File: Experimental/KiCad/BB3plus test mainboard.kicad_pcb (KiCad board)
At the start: 4 copper layers, 180.5 x 176 mm, 292 parts, among them IC1 SN74HCS02PWR, IC10 TPS62933ODRLR, IC11 FUSB303BTMX, IC12 TPS2068E, IC13 RT9742SNGV, IC14 TPD4E001DRLR, IC15 TPD4E001DRLR, IC16 TPD12S016PWR, IC17 MIC2026A-1YM-TR, IC18 TPD4E001DRLR, IC2 TPS3851H18EDRBR, IC3 M24C32-DFDW6TP, IC4 STM32G071R8T6, IC5 TPA6205A1DGN, IC6 SN74LVC1G14DBVR, IC7 LM64460CPPQRYFRQ1, IC8 TPS62933ODRLR, IC9 USB5816C-I/KD, Q1 DMP3013SFV-7, Q2 2N7002, Q3 2N7002, Q4 MMBT5401, Q5 MMBT5401, Q6 2N7002, Q7 DMP3013SFV-7, Q8 DMP3013SFV-7, SW1 WBL2UOAGQR05CLR, SW2 LP4EE1RBATY, SW3 PEC16-2215F-S0024, X1 1-2199230-6, X10 1001878410201TLF, X11 77313-802-20LF, X12 77313-802-20LF, X13 10018783-10101TLF, X14 5051102091, X15 TBP03R1-350-10BE, X3 571-0400, X4 GSP1.9101.1, X5 PJ-002BH-SMT-TR, X6 USB4056-03-A, X7 0862-1J1T-43-F, X8 SS-53000-002, X9 5051102091, Y1 32.768KHz, Y2 VXM7-9032-25M0000000

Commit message: Jumpers update
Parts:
- added JP15: ~, PCM_EEZ_SMD:JP3 shorted with 0R (0603) 2-3, F.Cu at (397.3, 119.3)
- added JP16: ~, PCM_EEZ_SMD:JP3 shorted with 0R (0603) 2-3, F.Cu at (397.3, 120.6)
- JP14, JP2, JP6: value ~ -> 0R
- moved C7 3.13 mm to (397.5, 114.3), turned to 0 degrees
- moved IC3 2.31 mm to (395.2, 116.8)
- renumbered C39 to C38, C38 to C39, C49 to C47, C50 to C48, C47 to C49, C48 to C50, R40 to R39, R39 to R40
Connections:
- net I2C_PU_BIAS renamed CM5_3V3
- Module1 pad 143: unconnected-(Module1B-HDMI1_HOTPLUG-Pad143) -> TFT_DVID_HPA
- Module1 pad 145: unconnected-(Module1B-HDMI1_SDA-Pad145) -> TFT_DVID_SDA
- Module1 pad 147: unconnected-(Module1B-HDMI1_SCL-Pad147) -> TFT_DVID_SCL
- Module1 pad 149: unconnected-(Module1B-HDMI1_CEC-Pad149) -> TFT_DVID_CEC
- X9 pad 14: unconnected-(X9-CTRL1-Pad14) -> TFT_DVID_HPA
- X9 pad 15: unconnected-(X9-CTRL2-Pad15) -> TFT_DVID_CEC
- X9 pad 20: SCL -> Net-(X9-SCL)
- X9 pad 21: SDA -> Net-(X9-SDA)
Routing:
- net TFT_DVID_SDA: track 0.00 -> 24.7 mm, vias 0 -> 2
- net TFT_DVID_HPA: track 0.00 -> 24.7 mm, vias 0 -> 2
- net TFT_DVID_CEC: track 0.00 -> 22.6 mm, vias 0 -> 2
- net TFT_DVID_SCL: track 0.00 -> 21.9 mm, vias 0 -> 2
- net Net-(TR1-+): track 13.3 -> 4.72 mm
- net Net-(X9-SCL): track 0.00 -> 4.53 mm
- net Net-(X9-SDA): track 0.00 -> 3.18 mm
- net SCL: track 213.2 -> 215.6 mm
- net SDA: track 216.0 -> 218.2 mm
- net GND: track 87.1 -> 87.9 mm
- net REAR_DVID_HPA: track 109.2 -> 108.5 mm
- net REAR_DVID_CEC: track 107.4 -> 106.7 mm
- net PE: track 800.5 -> 801.1 mm
- net +3V3: track 92.4 -> 93.1 mm
- added copper zone on F.Cu, net Net-(TR1-+)

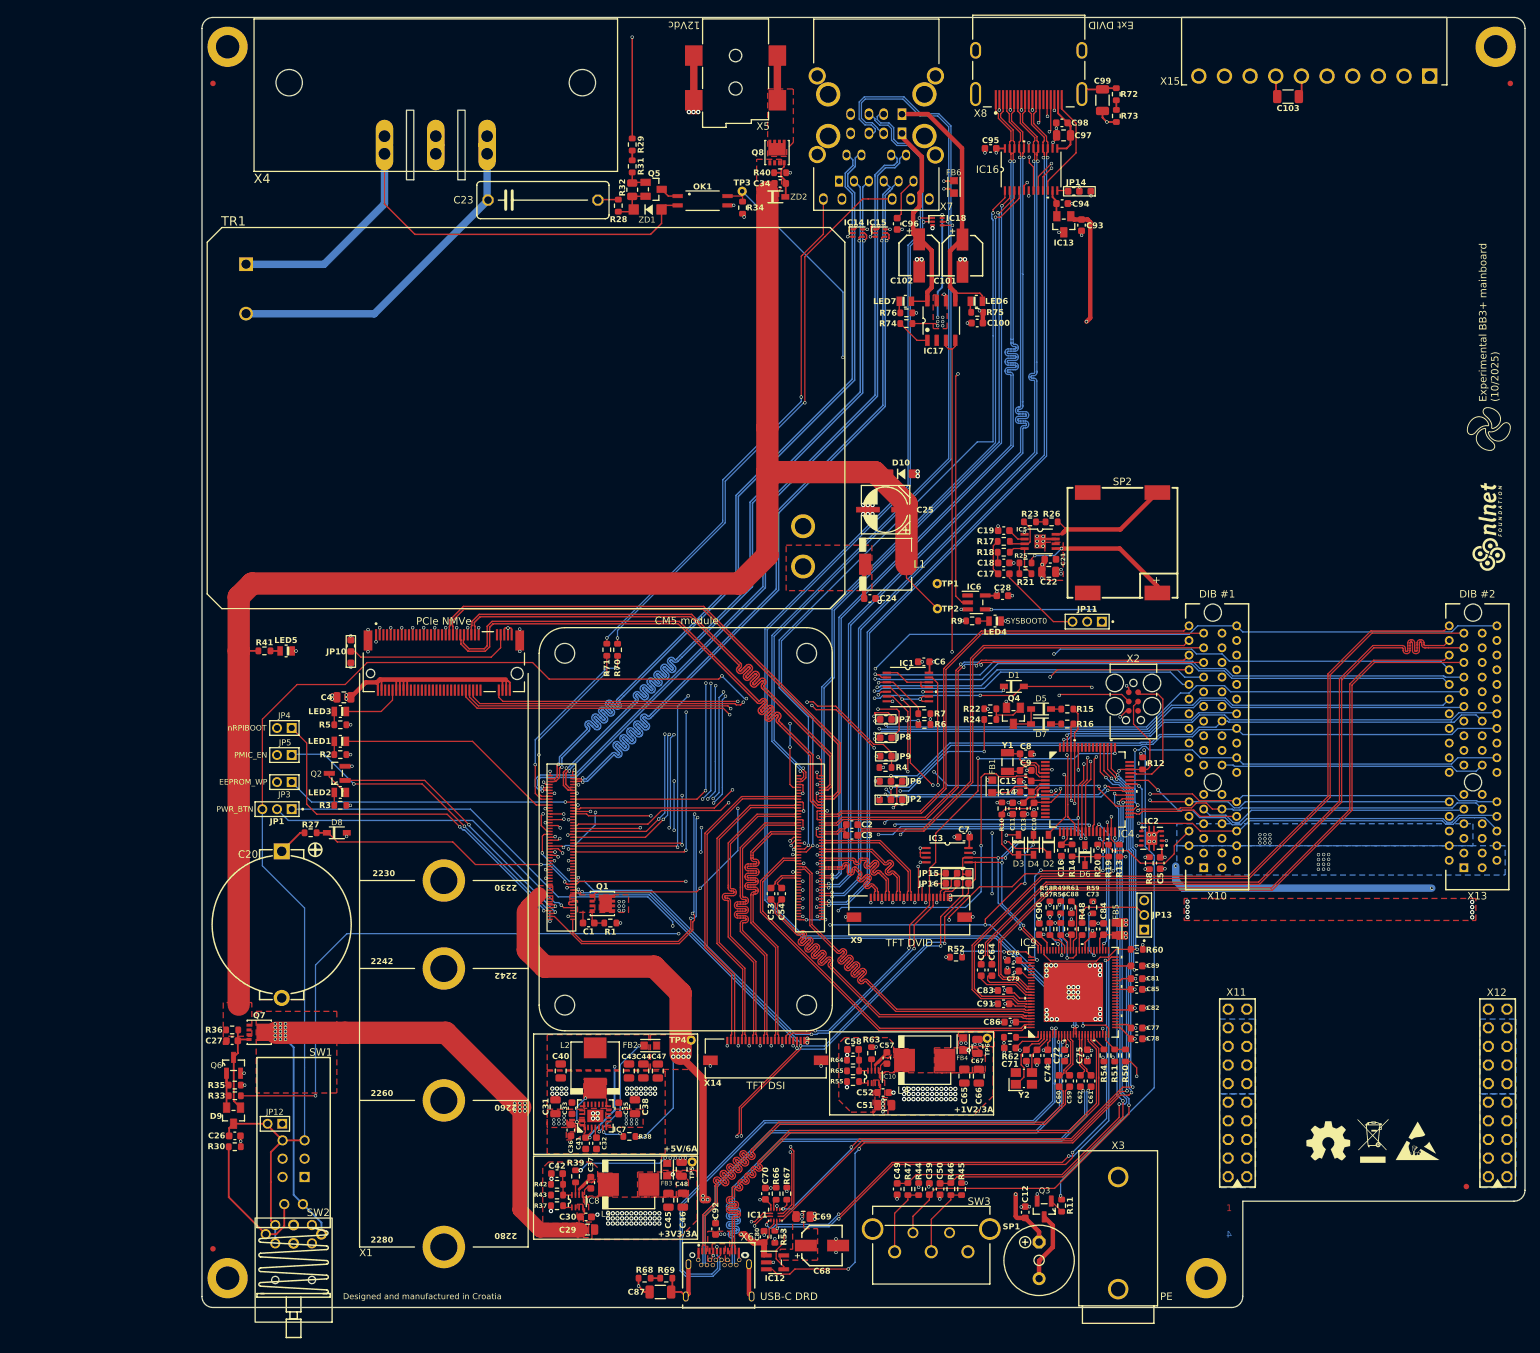
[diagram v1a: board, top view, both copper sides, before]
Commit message: Power switch modified
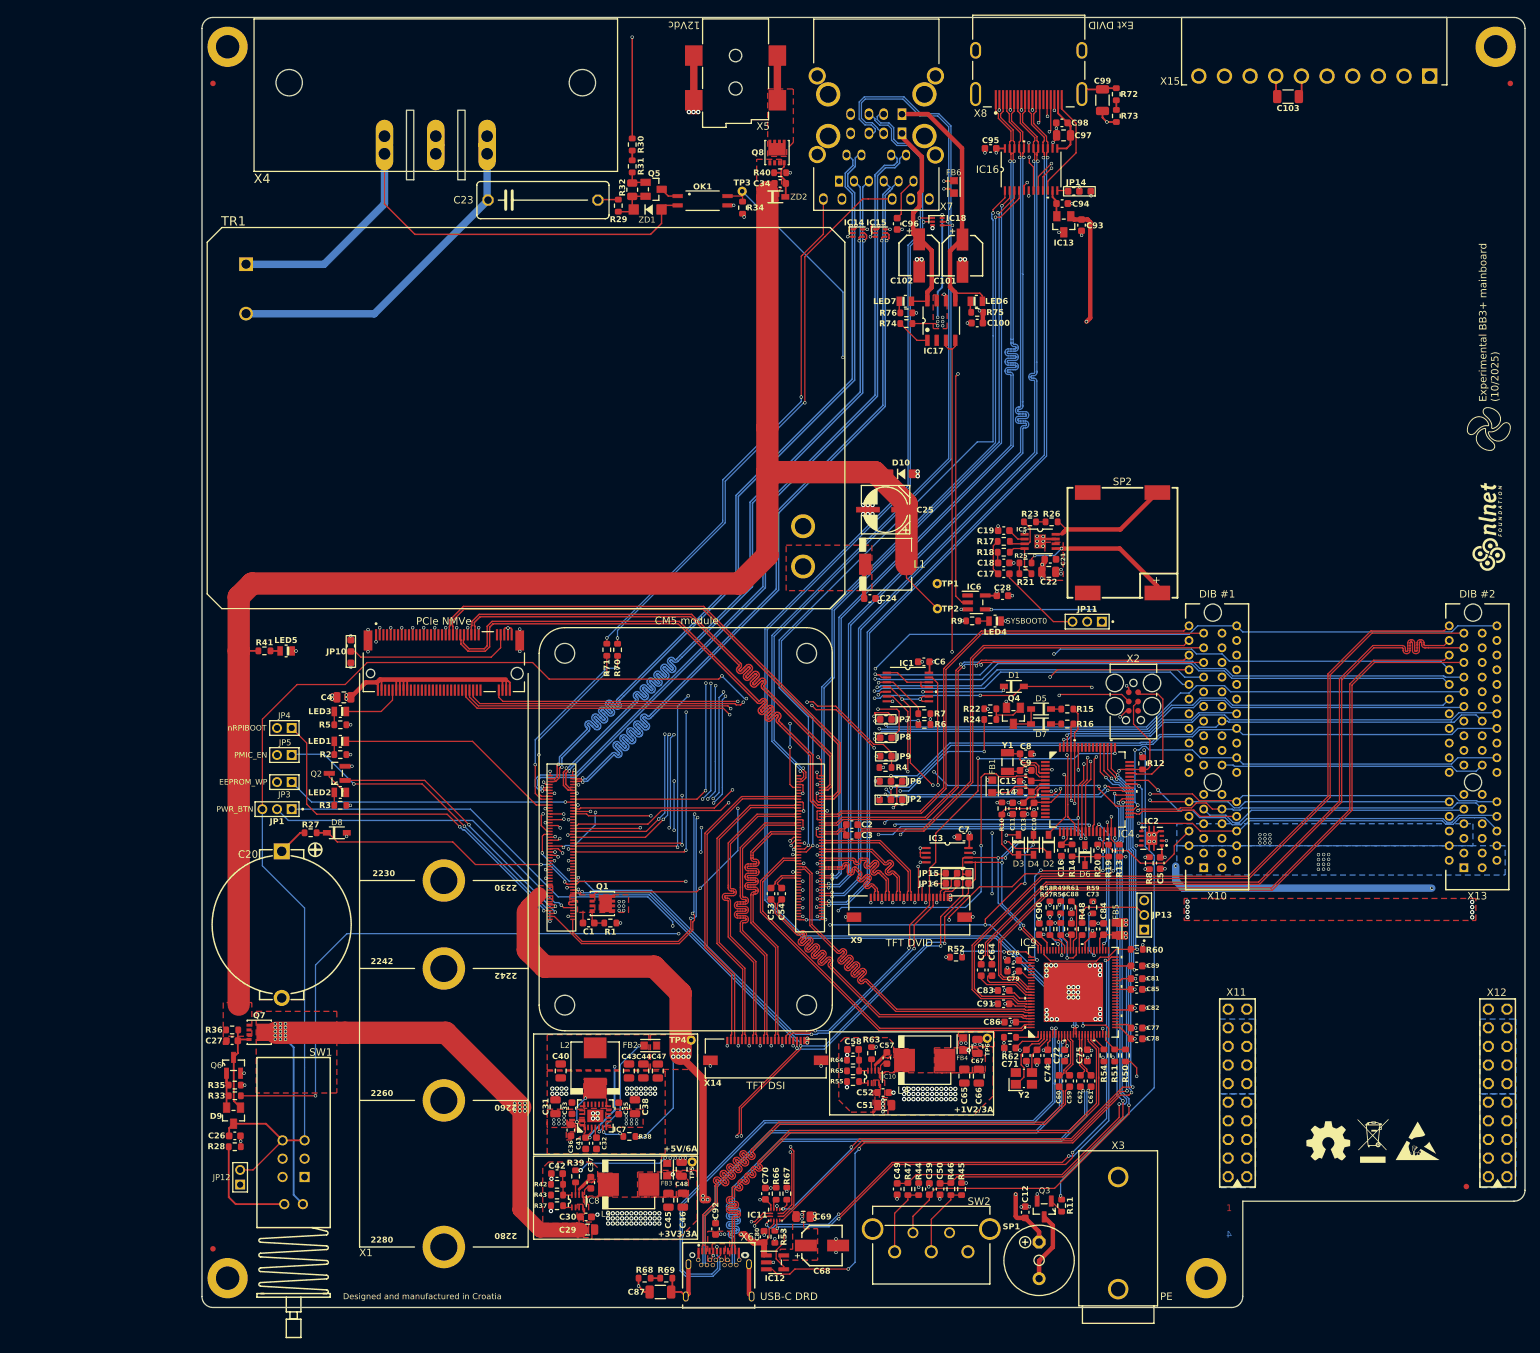
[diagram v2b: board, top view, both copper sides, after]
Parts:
- removed the SW2 at (306.0, 168.5)
- X13: value 10018783-10101TLF -> 1001878410201TLF
- moved JP12 8.70 mm to (298.7, 160.7), turned to 90 degrees
- renumbered R30 to R28, R28 to R29, R29 to R30, SW3 to SW2
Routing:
- net POWER_SW: track 227.1 -> 219.5 mm
- net Net-(R28-Pad2): track 20.4 -> 14.9 mm
- net +12V: track 231.0 -> 225.9 mm
